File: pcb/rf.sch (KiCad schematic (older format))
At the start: 20 parts

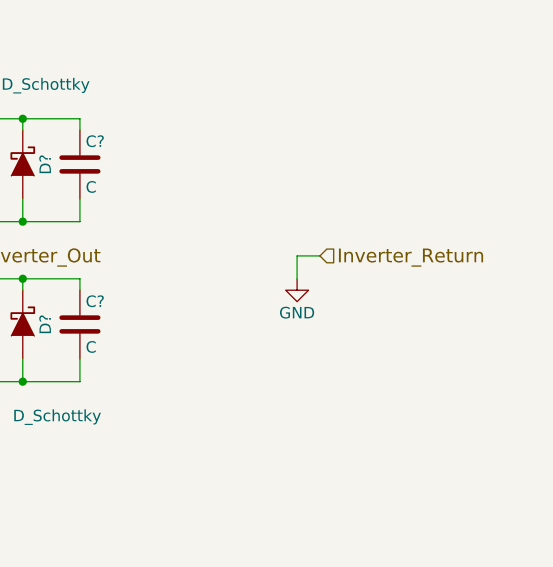
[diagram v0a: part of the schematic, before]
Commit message: added measurements and simulation
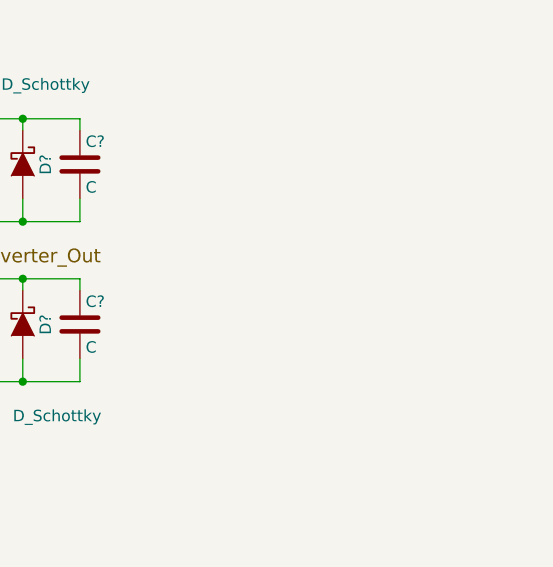
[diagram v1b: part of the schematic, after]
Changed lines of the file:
@@
 Text Notes 1750 4800 0    60   ~ 0
 Decoupling
-Text HLabel 6000 3100 2    60   Input ~ 0
-Inverter_Return
-$Comp
-L GND #PWR?
-U 1 1 570578C9
-P 5900 3200
-F 0 "#PWR?" H 5900 2950 50  0001 C CNN
-F 1 "GND" H 5900 3050 50  0000 C CNN
-F 2 "" H 5900 3200 50  0000 C CNN
-F 3 "" H 5900 3200 50  0000 C CNN
-	1    5900 3200
-	1    0    0    -1
-$EndComp
-Wire Wire Line
-	6000 3100 5900 3100
-Wire Wire Line
-	5900 3100 5900 3200
 $EndSCHEMATC

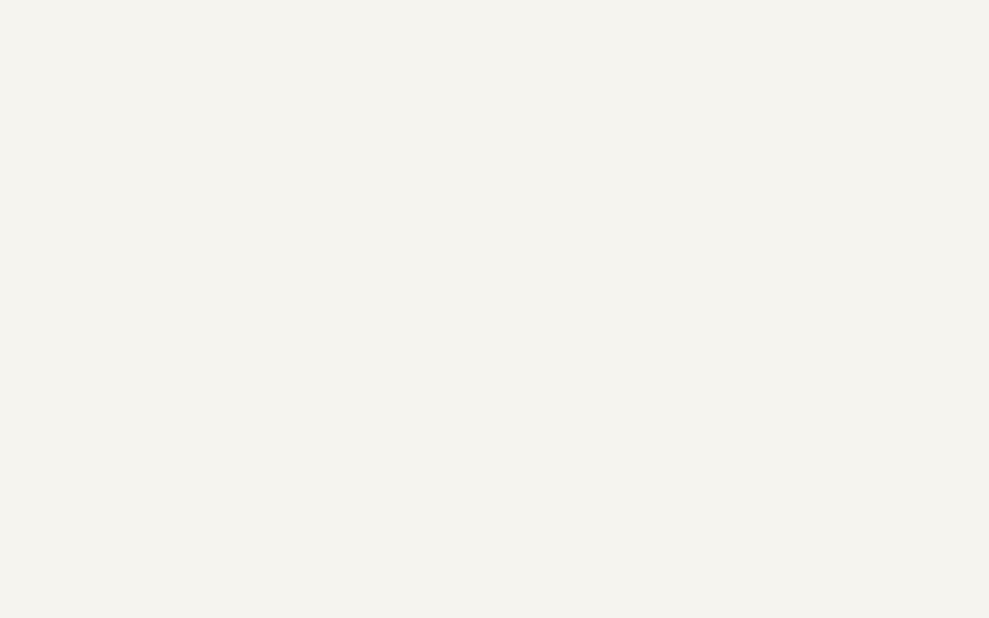
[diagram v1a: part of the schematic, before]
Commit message: new GaN test board
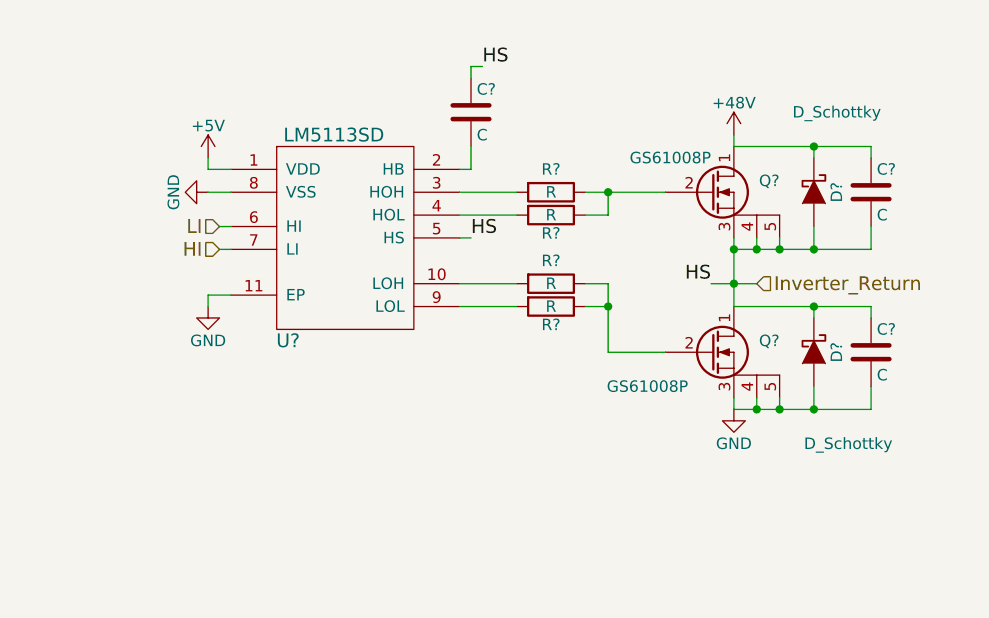
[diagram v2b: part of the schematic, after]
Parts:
- added C? (x3): C, symbol C
- added D? (x2): D_Schottky, symbol D_Schottky
- added Q? (x2): GS61008P, symbol GS61008P
- added R? (x4): R, symbol R
- added U?: LM5113SD, symbol LM5113SD
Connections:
- net +48V: now also C?.1, D?.1 (K), Q?.1 (D)
- net +5V: now also U?.1 (VDD)
- net GND: now also C?.2, D?.2 (A), Q?.3 (SS), Q?.4 (S), Q?.5 (TH), U?.11 (EP), U?.8 (VSS)
- net HI: now also U?.7 (LI)
- net Inverter_Out: now also C?.1, C?.1, C?.2, D?.1 (K), D?.2 (A), Q?.1 (D), Q?.3 (SS), Q?.4 (S), Q?.5 (TH), U?.5 (HS)
- net LI: now also U?.6 (HI)
- new net: Q?.2 (G), R?.1, R?.1 (x2)
- new net: R?.2, U?.10 (LOH)
- new net: C?.2, U?.2 (HB)
- new net: R?.2, U?.3 (HOH)
- new net: R?.2, U?.4 (HOL)
- new net: R?.2, U?.9 (LOL)
